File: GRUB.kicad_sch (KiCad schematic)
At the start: 51 parts, among them J2 External Digital Controller, J3 Timer or foot switch, Q1 2N3904, Q2 2N3904, Q3 2N3904, Q5 2N3904, SW1 Red, SW2 UV, SW3 Blue, SW4 1) Focus 2) Safelight 3) Colo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, SW6 Green, U1 A009 BuckBlock or LDDS-HWB, U13 PC847, U2 A009 BuckBlock or LDDS-HWB, U3 A009 BuckBlock or LDDS-HWB, U4 PC847, U6 A009 BuckBlock or LDDS-HWB

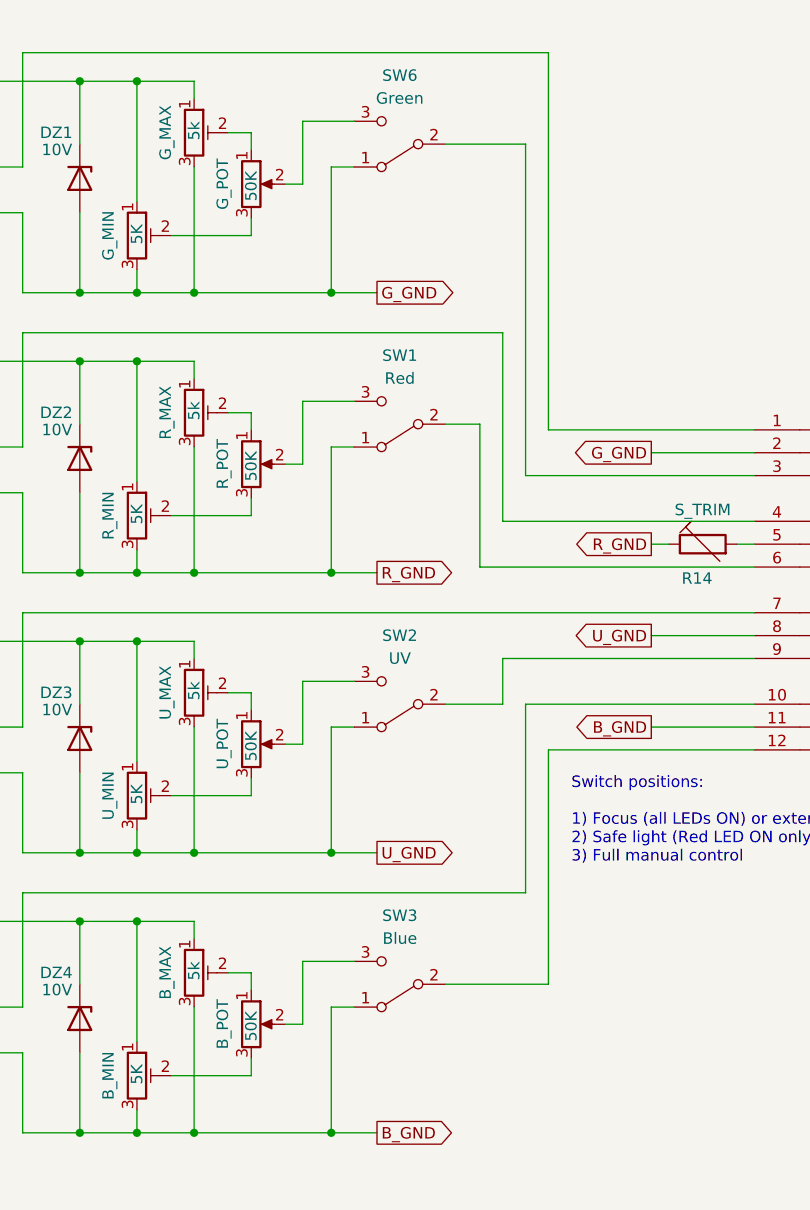
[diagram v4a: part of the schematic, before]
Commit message: Given the proper names to the LEDs activation switches
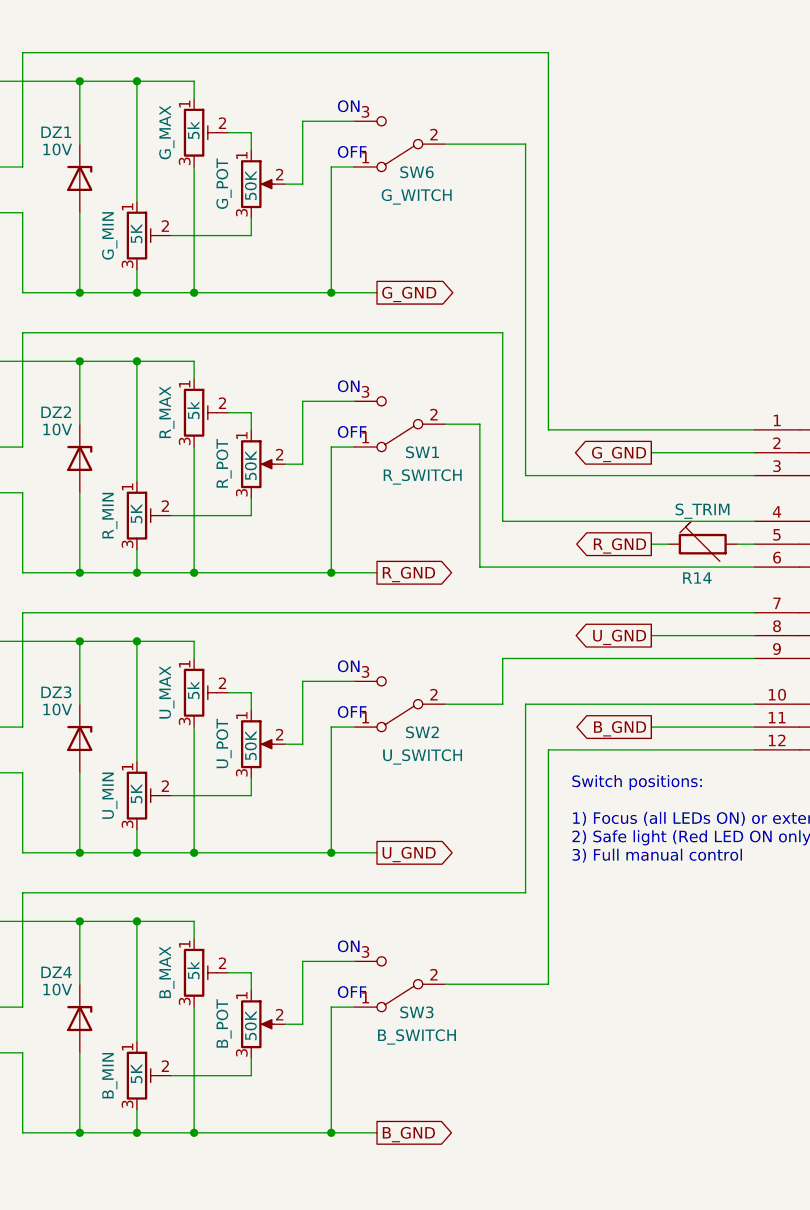
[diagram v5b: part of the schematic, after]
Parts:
- SW1: value Red -> R_SWITCH
- SW2: value UV -> U_SWITCH
- SW3: value Blue -> B_SWITCH
- SW6: value Green -> G_WITCH
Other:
- note added: "OFF"
- note added: "ON"
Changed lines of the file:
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@@
     (stroke (width 0) (type default))
+  )
+  (text "OFF" (at 116.205 123.19 0)
+    (effects (font (size 1.27 1.27)) (justify left bottom))
   )
   (text "Switch positions:\n\n1) Focus (all LEDs ON) or external control\n2) Safe light (Red LED ON only)\n3) Full manual control"
@@
     (effects (font (size 1.27 1.27)) (justify right bottom))
   )
+  (text "OFF" (at 116.205 60.96 0)
+    (effects (font (size 1.27 1.27)) (justify left bottom))
+  )
   (text "R_PWM" (at 27.305 67.31 0)
     (effects (font (size 1.27 1.27)) (justify right bottom))
@@
     (effects (font (size 1.27 1.27)) (justify left bottom))
   )
+  (text "OFF" (at 116.205 29.845 0)
+    (effects (font (size 1.27 1.27)) (justify left bottom))
+  )
+  (text "ON" (at 116.205 55.88 0)
+    (effects (font (size 1.27 1.27)) (justify left bottom))
+  )
   (text "/OE" (at 27.305 74.93 0)
     (effects (font (size 1.27 1.27)) (justify right bottom))
+  )
+  (text "ON" (at 116.205 24.765 0)
+    (effects (font (size 1.27 1.27)) (justify left bottom))
+  )
+  (text "OFF" (at 116.205 92.075 0)
+    (effects (font (size 1.27 1.27)) (justify left bottom))
+  )
+  (text "ON" (at 116.205 86.995 0)
+    (effects (font (size 1.27 1.27)) (justify left bottom))
+  )
+  (text "ON" (at 116.205 118.11 0)
+    (effects (font (size 1.27 1.27)) (justify left bottom))
   )
   (text "U_PWM" (at 27.305 69.85 0)
@@
   (symbol (lib_id "Switch:SW_SPDT") (at 123.19 59.055 180) (unit 1)
     (in_bom yes) (on_board yes) (dnp no)
-    (property "Reference" "SW1" (at 123.19 51.435 0)
-      (effects (font (size 1.27 1.27)))
-    )
-    (property "Value" "Red" (at 123.19 53.975 0)
+    (property "Reference" "SW1" (at 125.73 62.23 0)
+      (effects (font (size 1.27 1.27)))
+    )
+    (property "Value" "R_SWITCH" (at 125.73 64.77 0)
       (effects (font (size 1.27 1.27)))
     )
@@
   (symbol (lib_id "Switch:SW_SPDT") (at 123.19 121.285 180) (unit 1)
     (in_bom yes) (on_board yes) (dnp no)
-    (property "Reference" "SW3" (at 123.19 113.665 0)
-      (effects (font (size 1.27 1.27)))
-    )
-    (property "Value" "Blue" (at 123.19 116.205 0)
+    (property "Reference" "SW3" (at 125.095 124.46 0)
+      (effects (font (size 1.27 1.27)))
+    )
+    (property "Value" "B_SWITCH" (at 125.095 127 0)
       (effects (font (size 1.27 1.27)))
     )
@@
   (symbol (lib_id "Switch:SW_SPDT") (at 123.19 27.94 180) (unit 1)
     (in_bom yes) (on_board yes) (dnp no)
-    (property "Reference" "SW6" (at 123.19 20.32 0)
-      (effects (font (size 1.27 1.27)))
-    )
-    (property "Value" "Green" (at 123.19 22.86 0)
+    (property "Reference" "SW6" (at 125.095 31.115 0)
+      (effects (font (size 1.27 1.27)))
+    )
+    (property "Value" "G_WITCH" (at 125.095 33.655 0)
       (effects (font (size 1.27 1.27)))
     )
@@
   (symbol (lib_id "Switch:SW_SPDT") (at 123.19 90.17 180) (unit 1)
     (in_bom yes) (on_board yes) (dnp no)
-    (property "Reference" "SW2" (at 123.19 82.55 0)
-      (effects (font (size 1.27 1.27)))
-    )
-    (property "Value" "UV" (at 123.19 85.09 0)
-      (effects (font (size 1.27 1.27)))
-    )
+    (property "Reference" "SW2" (at 125.73 93.345 0)
+      (effects (font (size 1.27 1.27)))
+    )
+    (property "Value" "U_SWITCH" (at 125.73 95.885 0)
+      (effects (font (size 1.27 1.27)))
+    )

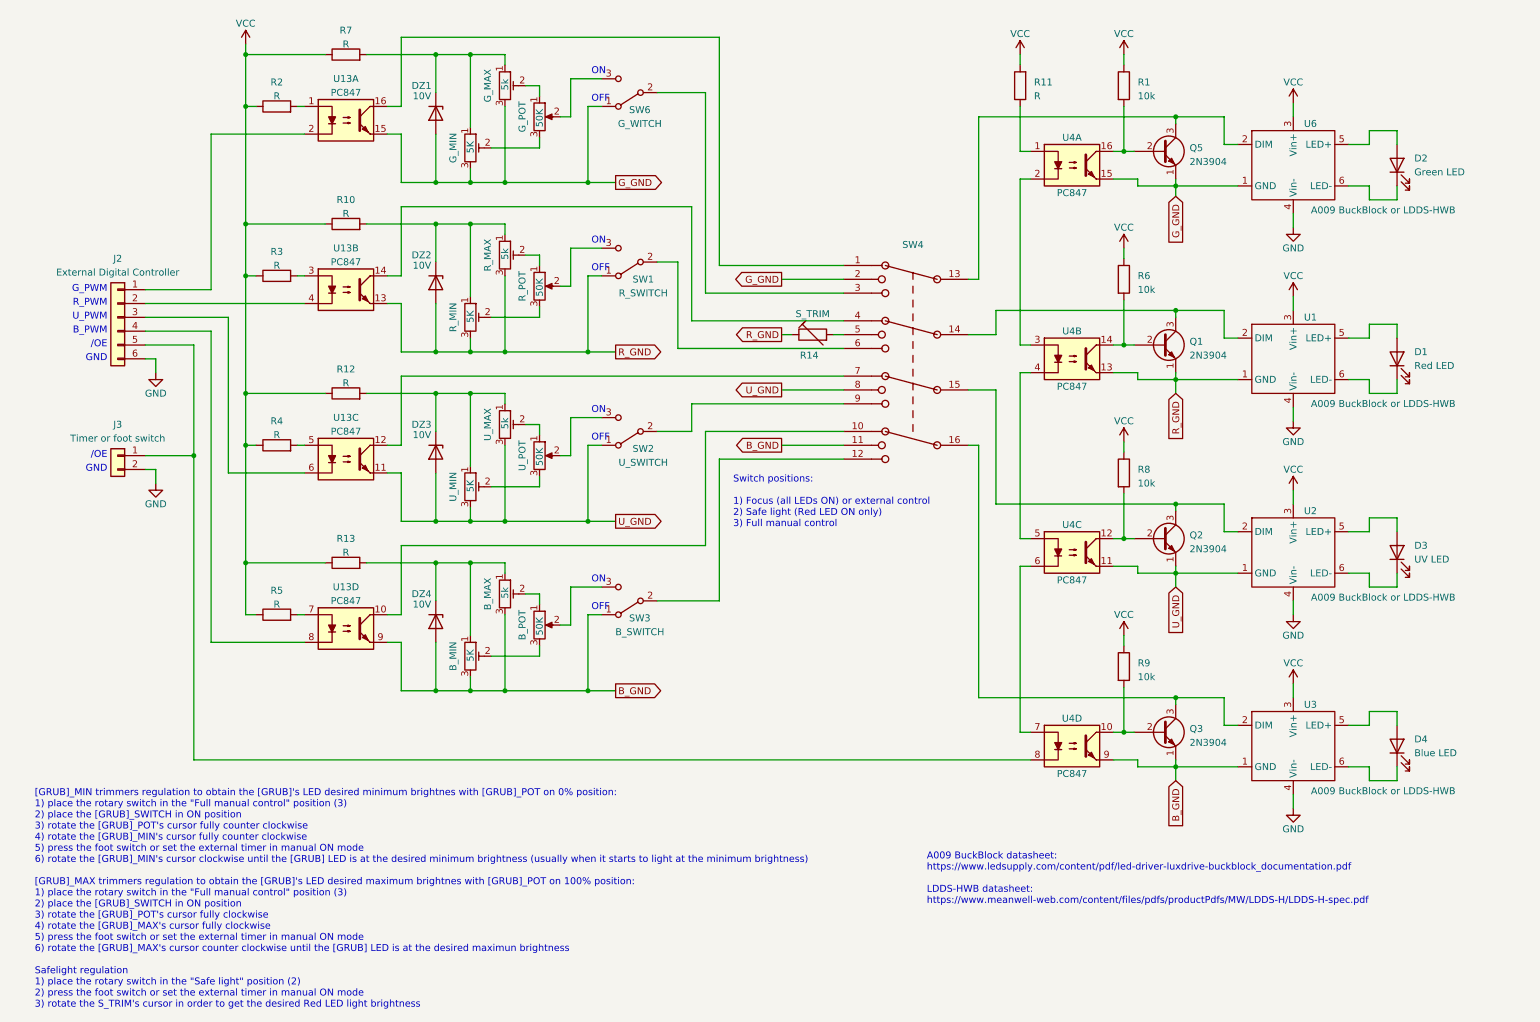
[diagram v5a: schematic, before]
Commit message: Using single PC817 optocoupler instead of cumulative PC847
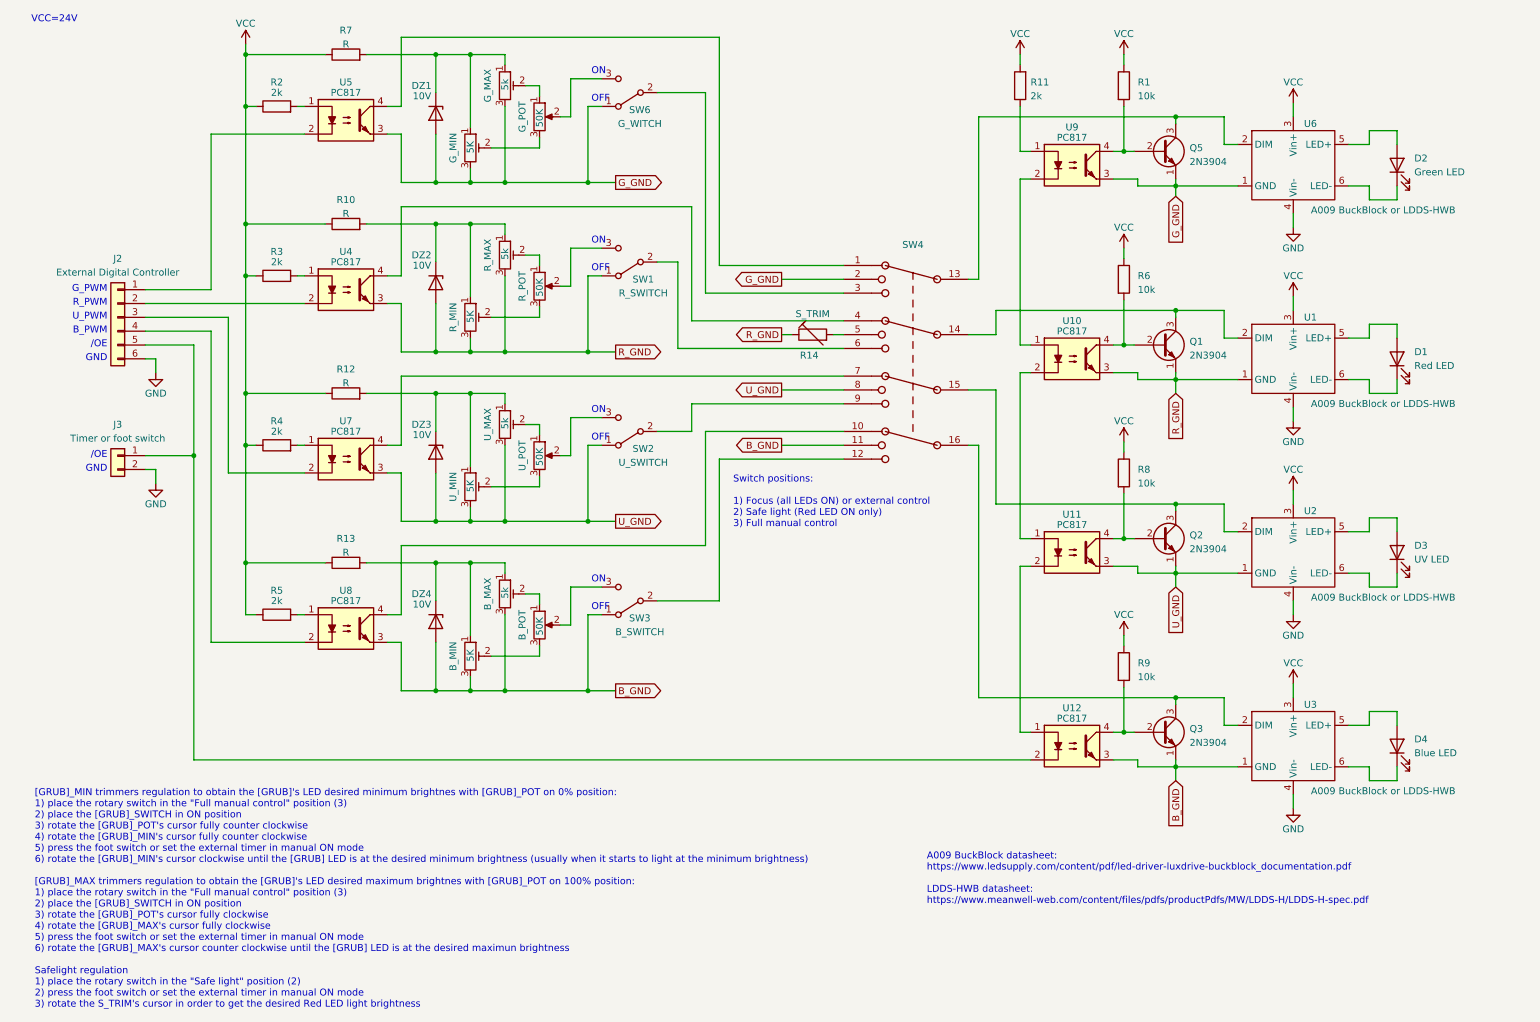
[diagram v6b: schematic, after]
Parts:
- removed U13, U4: PC847, Housings_DIP:DIP-16_W7.62mm, symbol opto:PC847
- added U10, U11, U12, U4, U5, U7, U8, U9: PC817, Housings_DIP:DIP-4_W7.62mm, symbol opto:PC817
- R11, R2, R3, R4, R5: value R -> 2k
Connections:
- net B_GND: now also U12.3, U8.3
- net G_GND: now also U5.3, U9.3
- net R_GND: now also U10.3, U4.3
- net U_GND: now also U11.3, U7.3
- net at J2.1 (Pin_1): now also U5.2
- net at J2.2 (Pin_2): now also U4.2
- net at J2.3 (Pin_3): now also U7.2
- net at J2.4 (Pin_4): now also U8.2
- net at J2.5 (Pin_5), J3.1 (Pin_1): now also U12.2
- net at R2.2: now also U5.1
- net at SW4.4: now also U4.4
- net at R3.2: now also U4.1
- net at Q1.2 (B), R6.2: now also U10.4
- net at Q2.2 (B), R8.2: now also U11.4
- net at Q3.2 (B), R9.2: now also U12.4
- net at R11.1: now also U9.1
- net at Q5.2 (B), R1.2: now also U9.4
- net at SW4.1: now also U5.4
- net at SW4.10: now also U8.4
- net at SW4.7: now also U7.4
- net at R4.2: now also U7.1
- net at R5.2: now also U8.1
- new net: U10.2, U11.1
- new net: U11.2, U12.1
- new net: U10.1, U9.2
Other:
- note added: "VCC=24V"

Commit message: Safe light regulated by voltage, not by resistor
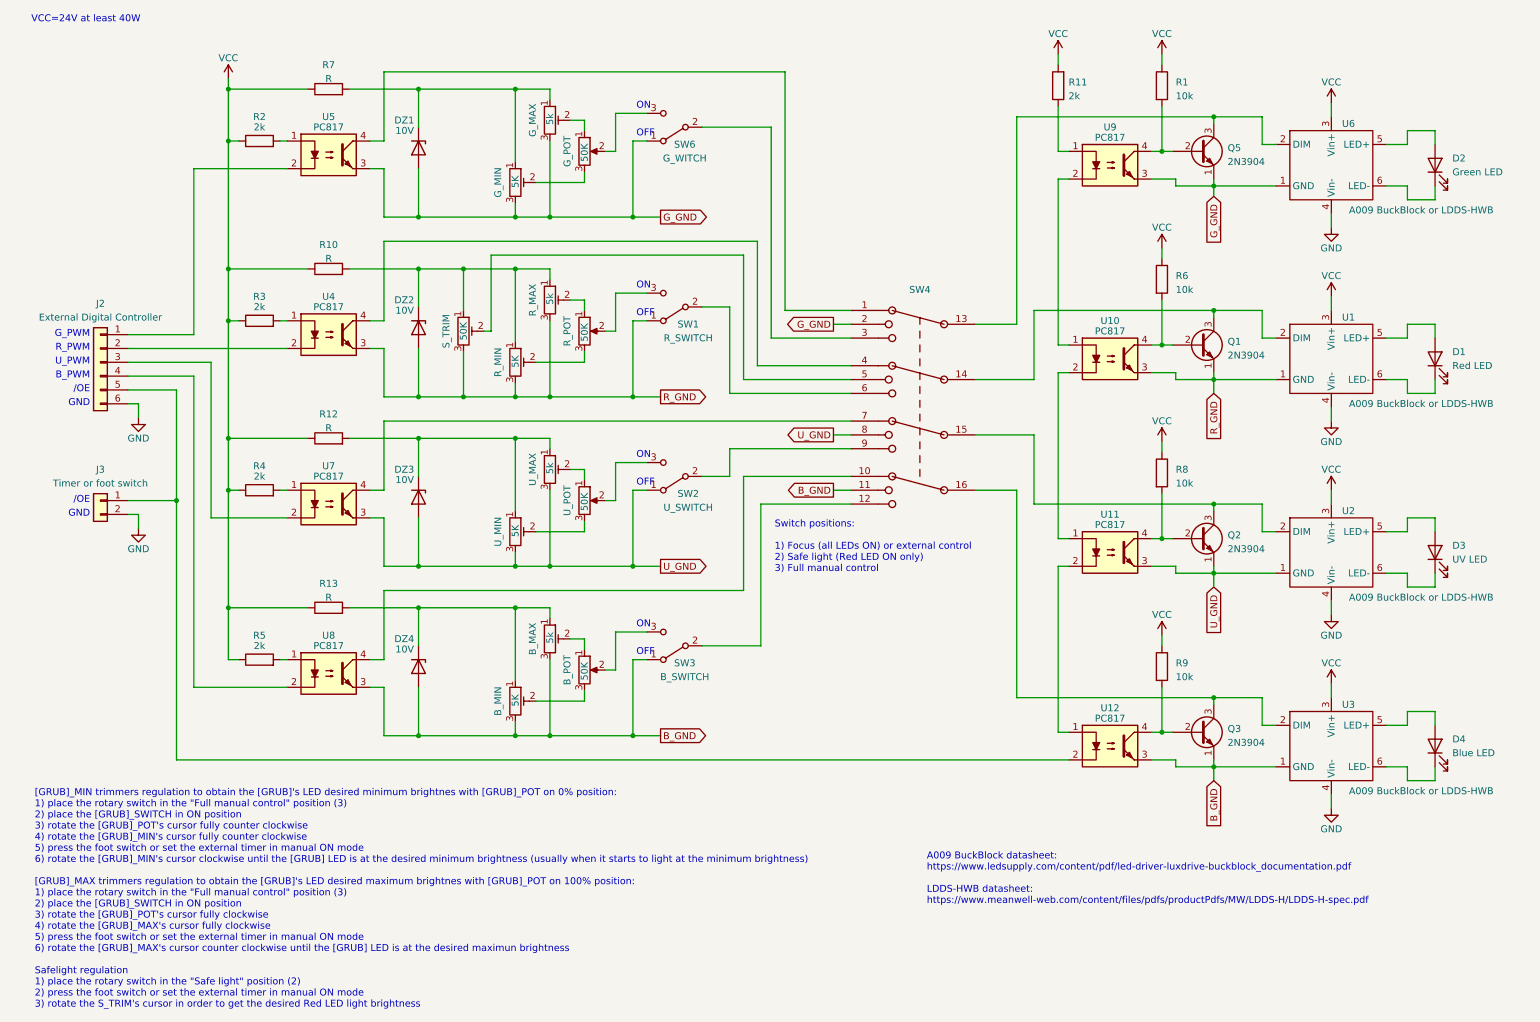
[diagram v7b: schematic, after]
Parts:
- removed R14: S_TRIM, symbol Device:RTRIM
- added S_TRIM: 50K, symbol Device:R_POT_TRIM
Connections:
- net R_GND: now also S_TRIM.3
- net at DZ2.1 (K), R10.2, R_MAX.1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: now also S_TRIM.1
- net at SW4.5: now also S_TRIM.2
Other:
- note added: "VCC=24V at least 40W"
- note removed: "VCC=24V"
- moved on the sheet: B_MAX, B_MIN, B_POT, D1, D2, D3, D4, DZ1, DZ2, DZ3, DZ4, G_MAX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
